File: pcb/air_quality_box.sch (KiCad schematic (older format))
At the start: 10 parts

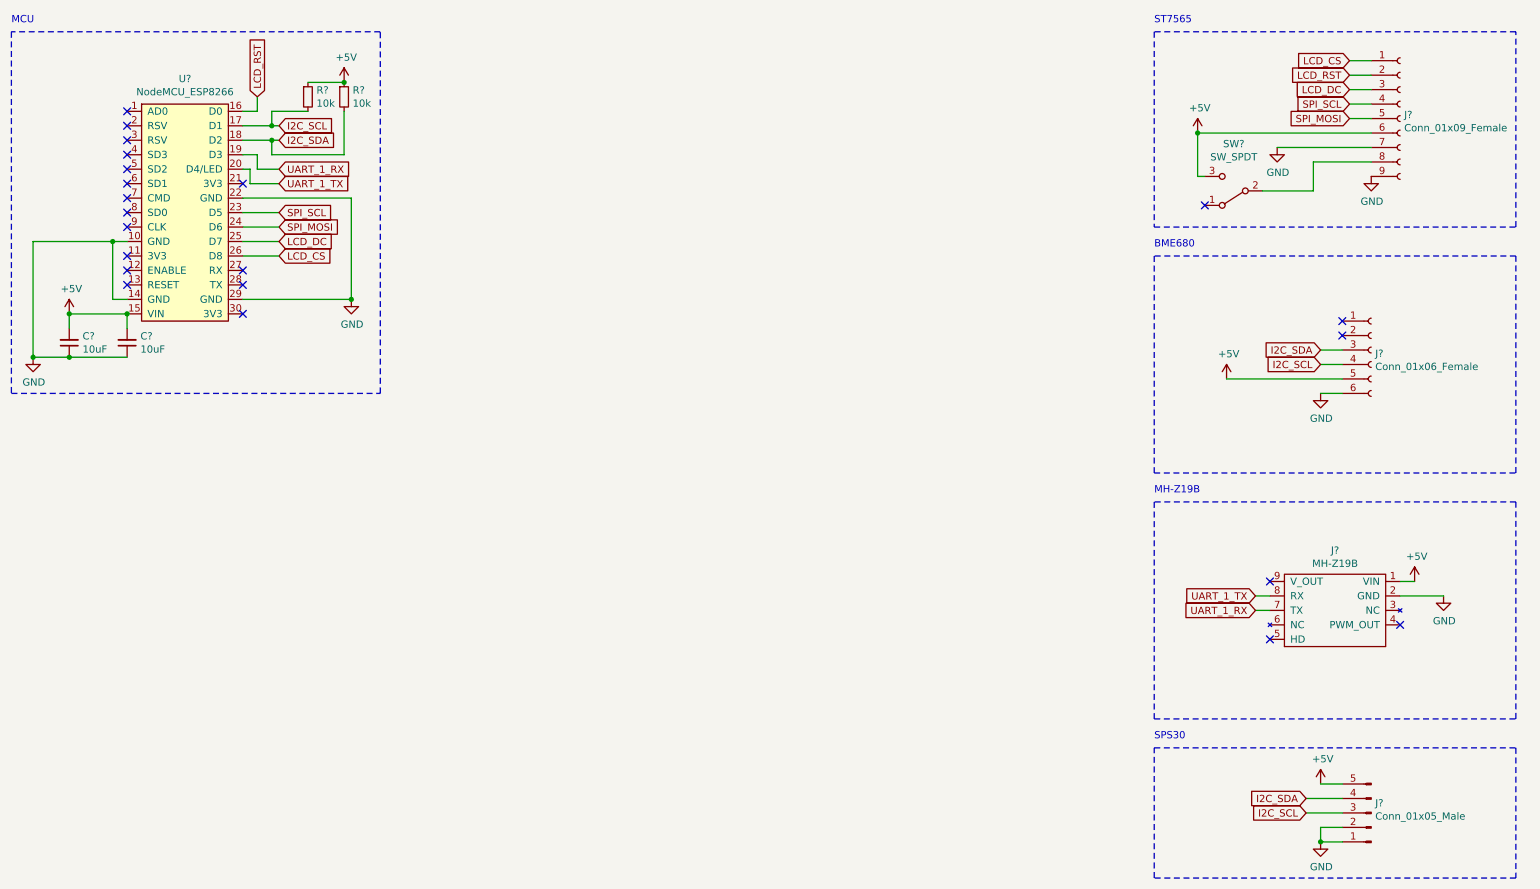
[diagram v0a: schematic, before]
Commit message: Create footprints
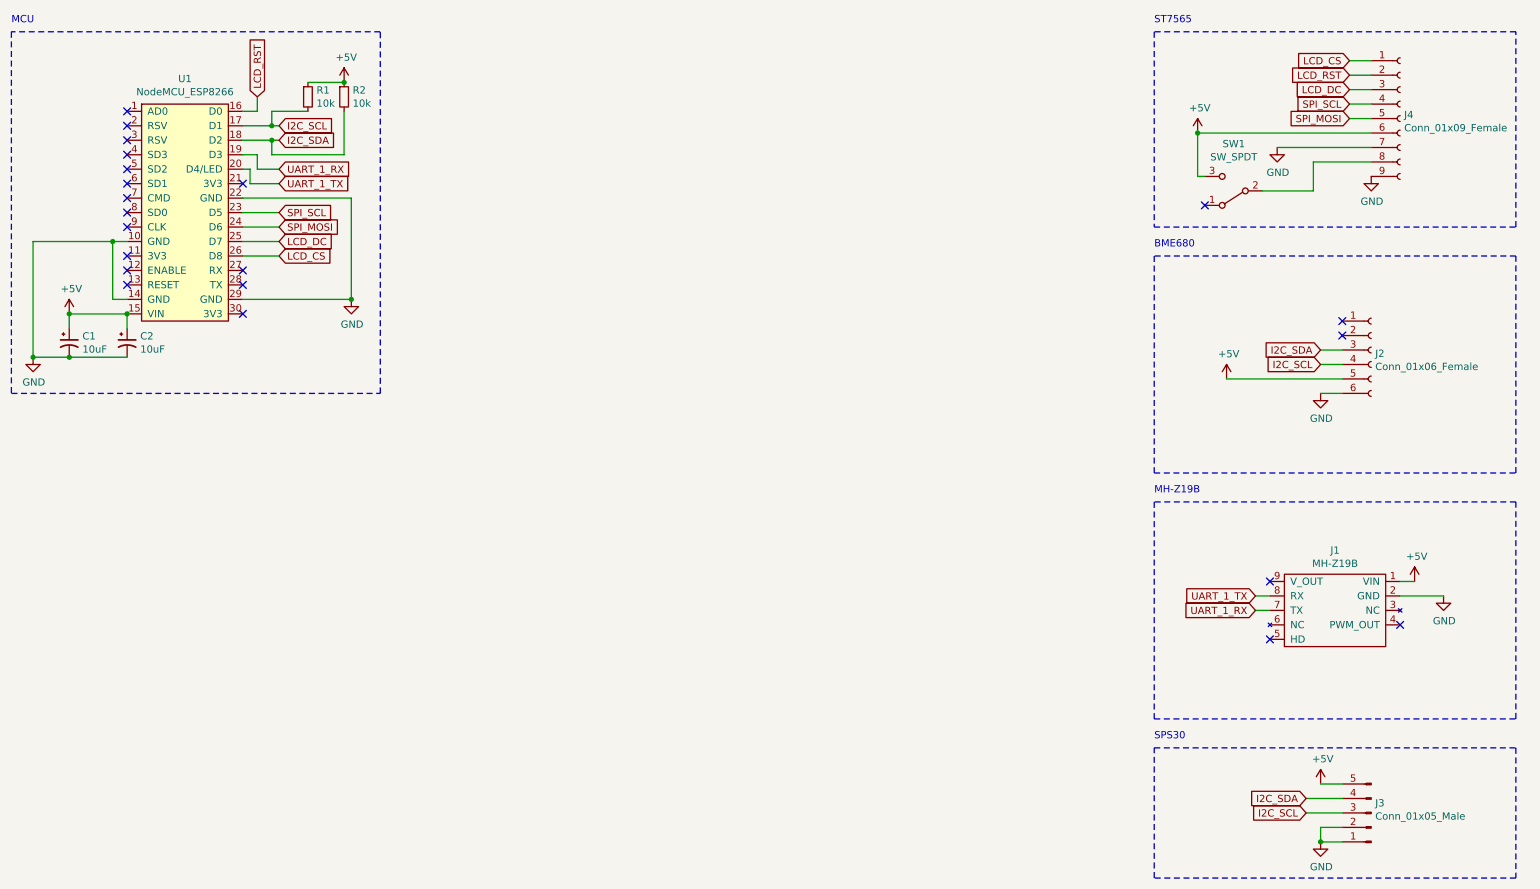
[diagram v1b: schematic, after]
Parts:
- removed C? (x2): 10uF, symbol Device:C_Small
- added C1, C2: 10uF, Capacitor_THT:CP_Radial_D5.0mm_P2.50mm, symbol Device:CP1_Small
- J1: renamed from J?; footprint (none) -> air_quality_box:MH-Z19B
- J2: renamed from J?; footprint (none) -> Connector_PinHeader_2.54mm:PinHeader_1x06_P2.54mm_Vertical
- J3: renamed from J?; footprint (none) -> air_quality_box:ZH_1.5mm_5P
- J4: renamed from J?; footprint (none) -> Connector_PinHeader_2.54mm:PinHeader_1x09_P2.54mm_Vertical
- R1, R2: renamed from R?; footprint (none) -> Resistor_THT:R_Axial_DIN0207_L6.3mm_D2.5mm_P10.16mm_Horizontal
- SW1: renamed from SW?; footprint (none) -> air_quality_box:switch
- U1: renamed from U?; footprint (none) -> air_quality_box:NodeMCU_ESP8266
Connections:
- net +5V: now also C1.1, C2.1
- net GND: now also C1.2, C2.2
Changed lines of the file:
@@
 	11000 2000 11000 650
 $Comp
-L Connector:Conn_01x06_Female J?
+L Connector:Conn_01x06_Female J2
 U 1 1 617833E7
 P 10000 2850
-F 0 "J?" H 10028 2826 50  0000 L CNN
+F 0 "J2" H 10028 2826 50  0000 L CNN
 F 1 "Conn_01x06_Female" H 10028 2735 50  0000 L CNN
-F 2 "" H 10000 2850 50  0001 C CNN
+F 2 "Connector_PinHeader_2.54mm:PinHeader_1x06_P2.54mm_Vertical" H 10000 2850 50  0001 C CNN
 F 3 "~" H 10000 2850 50  0001 C CNN
 	1    10000 2850
@@
 MH-Z19B
 $Comp
-L Connector:Conn_01x09_Female J?
+L Connector:Conn_01x09_Female J4
 U 1 1 6178C869
 P 10200 1250
-F 0 "J?" H 10228 1276 50  0000 L CNN
+F 0 "J4" H 10228 1276 50  0000 L CNN
 F 1 "Conn_01x09_Female" H 10228 1185 50  0000 L CNN
-F 2 "" H 10200 1250 50  0001 C CNN
+F 2 "Connector_PinHeader_2.54mm:PinHeader_1x09_P2.54mm_Vertical" H 10200 1250 50  0001 C CNN
 F 3 "~" H 10200 1250 50  0001 C CNN
 	1    10200 1250
@@
 	8500 6500 8500 5600
 $Comp
-L Connector:Conn_01x05_Male J?
+L Connector:Conn_01x05_Male J3
 U 1 1 61791B97
 P 10000 6050
-F 0 "J?" H 9972 5982 50  0000 R CNN
+F 0 "J3" H 9972 5982 50  0000 R CNN
 F 1 "Conn_01x05_Male" H 9972 6073 50  0000 R CNN
-F 2 "" H 10000 6050 50  0001 C CNN
+F 2 "air_quality_box:ZH_1.5mm_5P" H 10000 6050 50  0001 C CNN
 F 3 "~" H 10000 6050 50  0001 C CNN
 	1    10000 6050
@@
 $EndComp
 $Comp
-L power:+5V #PWR?
+L power:+5V #PWR0101
 U 1 1 61792ED0
 P 9650 5850
-F 0 "#PWR?" H 9650 5700 50  0001 C CNN
+F 0 "#PWR0101" H 9650 5700 50  0001 C CNN
 F 1 "+5V" H 9665 6023 50  0000 C CNN
 F 2 "" H 9650 5850 50  0001 C CNN
@@
 	9650 5850 9800 5850
 $Comp
-L power:GND #PWR?
+L power:GND #PWR0102
 U 1 1 617937E4
 P 9650 6250
-F 0 "#PWR?" H 9650 6000 50  0001 C CNN
+F 0 "#PWR0102" H 9650 6000 50  0001 C CNN
 F 1 "GND" H 9655 6077 50  0000 C CNN
 F 2 "" H 9650 6250 50  0001 C CNN
@@
 I2C_SCL
 $Comp
-L power:+5V #PWR?
+L power:+5V #PWR0103
 U 1 1 6179734D
 P 9000 3050
-F 0 "#PWR?" H 9000 2900 50  0001 C CNN
+F 0 "#PWR0103" H 9000 2900 50  0001 C CNN
 F 1 "+5V" H 9015 3223 50  0000 C CNN
 F 2 "" H 9000 3050 50  0001 C CNN
@@
 $EndComp
 $Comp
-L power:GND #PWR?
+L power:GND #PWR0104
 U 1 1 61797AE0
 P 9650 3150
-F 0 "#PWR?" H 9650 2900 50  0001 C CNN
+F 0 "#PWR0104" H 9650 2900 50  0001 C CNN
 F 1 "GND" H 9655 2977 50  0000 C CNN
 F 2 "" H 9650 3150 50  0001 C CNN
@@
 SPI_MOSI
 $Comp
-L power:+5V #PWR?
+L power:+5V #PWR0105
 U 1 1 6179C731
 P 8800 1350
-F 0 "#PWR?" H 8800 1200 50  0001 C CNN
+F 0 "#PWR0105" H 8800 1200 50  0001 C CNN
 F 1 "+5V" H 8815 1523 50  0000 C CNN
 F 2 "" H 8800 1350 50  0001 C CNN
@@
 $EndComp
 $Comp
-L power:GND #PWR?
+L power:GND #PWR0106
 U 1 1 6179CAFA
 P 9350 1450
-F 0 "#PWR?" H 9350 1200 50  0001 C CNN
+F 0 "#PWR0106" H 9350 1200 50  0001 C CNN
 F 1 "GND" H 9355 1277 50  0000 C CNN
 F 2 "" H 9350 1450 50  0001 C CNN
@@
 	10000 1450 9350 1450
 $Comp
-L power:GND #PWR?
+L power:GND #PWR0107
 U 1 1 6179E4E3
 P 10000 1650
-F 0 "#PWR?" H 10000 1400 50  0001 C CNN
+F 0 "#PWR0107" H 10000 1400 50  0001 C CNN
 F 1 "GND" H 10005 1477 50  0000 C CNN
 F 2 "" H 10000 1650 50  0001 C CNN
@@
 $EndComp
 $Comp
-L Switch:SW_SPDT SW?
+L Switch:SW_SPDT SW1
 U 1 1 617A0459
 P 9050 1750
-F 0 "SW?" H 9050 1425 50  0000 C CNN
+F 0 "SW1" H 9050 1425 50  0000 C CNN
 F 1 "SW_SPDT" H 9050 1516 50  0000 C CNN
-F 2 "" H 9050 1750 50  0001 C CNN
+F 2 "air_quality_box:switch" H 9050 1750 50  0001 C CNN
 F 3 "~" H 9050 1750 50  0001 C CNN
 	1    9050 1750
@@
 NoConn ~ 8850 1850
 $Comp
-L air_quality_box:MH-Z19B J?
+L air_quality_box:MH-Z19B J1
 U 1 1 617A2DC6
 P 9750 4650
-F 0 "J?" H 9750 4235 50  0000 C CNN
+F 0 "J1" H 9750 4235 50  0000 C CNN
 F 1 "MH-Z19B" H 9750 4326 50  0000 C CNN
-F 2 "" H 9600 4850 50  0001 C CNN
+F 2 "air_quality_box:MH-Z19B" H 9600 4850 50  0001 C CNN
 F 3 "" H 9600 4850 50  0001 C CNN
 	1    9750 4650
@@
 $EndComp
 $Comp
-L power:+5V #PWR?
+L power:+5V #PWR0108
 U 1 1 617A4292
 P 10300 4450
-F 0 "#PWR?" H 10300 4300 50  0001 C CNN
+F 0 "#PWR0108" H 10300 4300 50  0001 C CNN
 F 1 "+5V" H 10315 4623 50  0000 C CNN
 F 2 "" H 10300 4450 50  0001 C CNN
@@
 $EndComp
 $Comp
-L power:GND #PWR?
+L power:GND #PWR0109
 U 1 1 617A4775
 P 10500 4550
-F 0 "#PWR?" H 10500 4300 50  0001 C CNN
+F 0 "#PWR0109" H 10500 4300 50  0001 C CNN
 F 1 "GND" H 10505 4377 50  0000 C CNN
 F 2 "" H 10500 4550 50  0001 C CNN
@@
 	10000 1250 9850 1250
 $Comp
-L air_quality_box:NodeMCU_ESP8266 U?
+L air_quality_box:NodeMCU_ESP8266 U1
 U 1 1 617ABB77
 P 1800 1800
-F 0 "U?" H 1800 2625 50  0000 C CNN
+F 0 "U1" H 1800 2625 50  0000 C CNN
 F 1 "NodeMCU_ESP8266" H 1800 2534 50  0000 C CNN
-F 2 "" H 1800 1800 50  0001 C CNN
+F 2 "air_quality_box:NodeMCU_ESP8266" H 1800 1800 50  0001 C CNN
 F 3 "" H 1800 1800 50  0001 C CNN
 	1    1800 1800
@@
 NoConn ~ 2200 2600
 $Comp
-L power:+5V #PWR?
+L power:+5V #PWR0110
 U 1 1 617B2D88
 P 1000 2600
-F 0 "#PWR?" H 1000 2450 50  0001 C CNN
+F 0 "#PWR0110" H 1000 2450 50  0001 C CNN
 F 1 "+5V" H 1015 2773 50  0000 C CNN
 F 2 "" H 1000 2600 50  0001 C CNN
@@
 	1400 2600 1000 2600
 $Comp
-L power:GND #PWR?
+L power:GND #PWR0111
 U 1 1 617B43CF
 P 750 2900
-F 0 "#PWR?" H 750 2650 50  0001 C CNN
+F 0 "#PWR0111" H 750 2650 50  0001 C CNN
 F 1 "GND" H 755 2727 50  0000 C CNN
 F 2 "" H 750 2900 50  0001 C CNN
@@
 	2450 2200 2200 2200
 $Comp
-L power:GND #PWR?
+L power:GND #PWR0112
 U 1 1 617BFAC2
 P 2950 2500
-F 0 "#PWR?" H 2950 2250 50  0001 C CNN
+F 0 "#PWR0112" H 2950 2250 50  0001 C CNN
 F 1 "GND" H 2955 2327 50  0000 C CNN
 F 2 "" H 2950 2500 50  0001 C CNN
@@
 MCU
 $Comp
-L Device:C_Small C?
-U 1 1 617D72CD
-P 1000 2800
-F 0 "C?" H 908 2754 50  0000 R CNN
-F 1 "10uF" H 908 2845 50  0000 R CNN
-F 2 "" H 1000 2800 50  0001 C CNN
-F 3 "~" H 1000 2800 50  0001 C CNN
-	1    1000 2800
-	-1   0    0    1
-$EndComp
-$Comp
-L Device:C_Small C?
-U 1 1 617D810D
-P 1400 2800
-F 0 "C?" H 1308 2754 50  0000 R CNN
-F 1 "10uF" H 1308 2845 50  0000 R CNN
-F 2 "" H 1400 2800 50  0001 C CNN
-F 3 "~" H 1400 2800 50  0001 C CNN
-	1    1400 2800
-	-1   0    0    1
-$EndComp
-$Comp
-L Device:R_Small R?
+L Device:R_Small R2
 U 1 1 617E554F
 P 2900 1100
-F 0 "R?" H 2959 1146 50  0000 L CNN
+F 0 "R2" H 2959 1146 50  0000 L CNN
 F 1 "10k" H 2959 1055 50  0000 L CNN
-F 2 "" H 2900 1100 50  0001 C CNN
+F 2 "Resistor_THT:R_Axial_DIN0207_L6.3mm_D2.5mm_P10.16mm_Horizontal" H 2900 1100 50  0001 C CNN
 F 3 "~" H 2900 1100 50  0001 C CNN
 	1    2900 1100
@@
 	3150 3150 3150 650
 $Comp
-L Device:R_Small R?
+L Device:R_Small R1
 U 1 1 617F1057
 P 2650 1100
-F 0 "R?" H 2709 1146 50  0000 L CNN
+F 0 "R1" H 2709 1146 50  0000 L CNN
 F 1 "10k" H 2709 1055 50  0000 L CNN
-F 2 "" H 2650 1100 50  0001 C CNN
+F 2 "Resistor_THT:R_Axial_DIN0207_L6.3mm_D2.5mm_P10.16mm_Horizontal" H 2650 1100 50  0001 C CNN
 F 3 "~" H 2650 1100 50  0001 C CNN
 	1    2650 1100
@@
 	2650 1000 2900 1000
 $Comp
-L power:+5V #PWR?
+L power:+5V #PWR0113
 U 1 1 617F67A9
 P 2900 1000
-F 0 "#PWR?" H 2900 850 50  0001 C CNN
+F 0 "#PWR0113" H 2900 850 50  0001 C CNN
 F 1 "+5V" H 2915 1173 50  0000 C CNN
 F 2 "" H 2900 1000 50  0001 C CNN
@@
 	2300 1200 2200 1200
 Wire Wire Line
-	1400 2900 1000 2900
-Connection ~ 1000 2900
-Wire Wire Line
-	1000 2900 750  2900
-Wire Wire Line
 	1000 2600 1000 2700
 Connection ~ 1000 2600
@@
 Connection ~ 1300 2100
 Connection ~ 750  2900
+$Comp
+L Device:CP1_Small C1
+U 1 1 617A08F4
+P 1000 2800
+F 0 "C1" H 1091 2846 50  0000 L CNN
+F 1 "10uF" H 1091 2755 50  0000 L CNN
+F 2 "Capacitor_THT:CP_Radial_D5.0mm_P2.50mm" H 1000 2800 50  0001 C CNN
+F 3 "~" H 1000 2800 50  0001 C CNN
+	1    1000 2800
+	1    0    0    -1
+$EndComp
+Wire Wire Line
+	750  2900 1000 2900
+Connection ~ 1000 2900
+Wire Wire Line
+	1000 2900 1400 2900
+$Comp
+L Device:CP1_Small C2
+U 1 1 617A1242
+P 1400 2800
+F 0 "C2" H 1491 2846 50  0000 L CNN
+F 1 "10uF" H 1491 2755 50  0000 L CNN
+F 2 "Capacitor_THT:CP_Radial_D5.0mm_P2.50mm" H 1400 2800 50  0001 C CNN
+F 3 "~" H 1400 2800 50  0001 C CNN
+	1    1400 2800
+	1    0    0    -1
+$EndComp
 $EndSCHEMATC

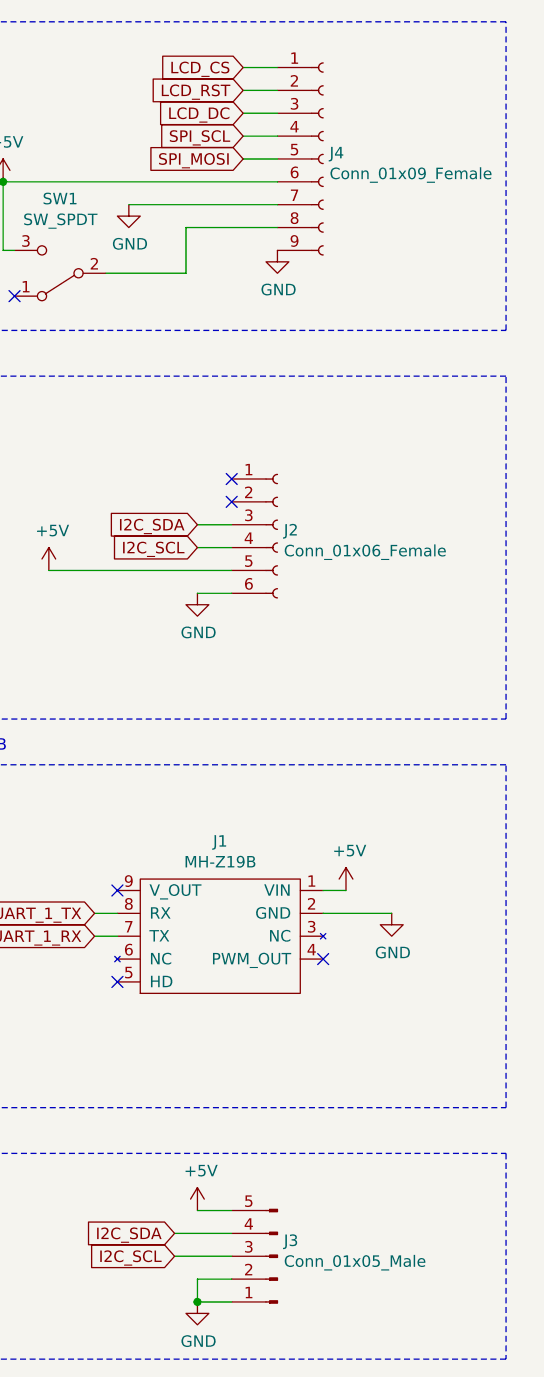
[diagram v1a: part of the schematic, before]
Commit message: Create basic board layout
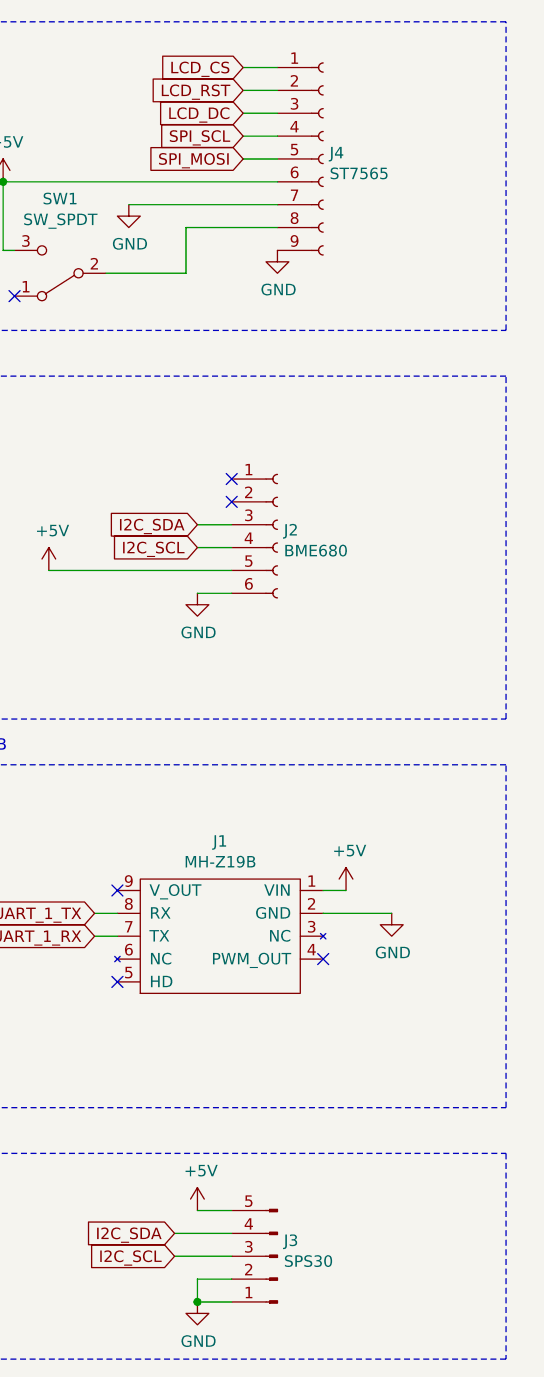
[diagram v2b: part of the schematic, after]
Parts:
- J2: value Conn_01x06_Female -> BME680
- J3: value Conn_01x05_Male -> SPS30
- J4: value Conn_01x09_Female -> ST7565
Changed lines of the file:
@@
 P 10000 2850
 F 0 "J2" H 10028 2826 50  0000 L CNN
-F 1 "Conn_01x06_Female" H 10028 2735 50  0000 L CNN
+F 1 "BME680" H 10028 2735 50  0000 L CNN
 F 2 "Connector_PinHeader_2.54mm:PinHeader_1x06_P2.54mm_Vertical" H 10000 2850 50  0001 C CNN
 F 3 "~" H 10000 2850 50  0001 C CNN
@@
 P 10200 1250
 F 0 "J4" H 10228 1276 50  0000 L CNN
-F 1 "Conn_01x09_Female" H 10228 1185 50  0000 L CNN
+F 1 "ST7565" H 10228 1185 50  0000 L CNN
 F 2 "Connector_PinHeader_2.54mm:PinHeader_1x09_P2.54mm_Vertical" H 10200 1250 50  0001 C CNN
 F 3 "~" H 10200 1250 50  0001 C CNN
@@
 P 10000 6050
 F 0 "J3" H 9972 5982 50  0000 R CNN
-F 1 "Conn_01x05_Male" H 9972 6073 50  0000 R CNN
+F 1 "SPS30" H 9972 6073 50  0000 R CNN
 F 2 "air_quality_box:ZH_1.5mm_5P" H 10000 6050 50  0001 C CNN
 F 3 "~" H 10000 6050 50  0001 C CNN
